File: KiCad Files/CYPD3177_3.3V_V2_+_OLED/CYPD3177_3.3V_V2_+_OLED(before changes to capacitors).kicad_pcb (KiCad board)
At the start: 4 copper layers, 64 x 17 mm, 93 parts, among them IC1 TPS16630RGER, IC2 TPS22992SRXNR, J1 USB_C_USB2.0_16P, J2 Conn_01x02_Pin, J3 Conn_02x05_Odd_Even, J4 Conn_02x05_Odd_Even, J5 0.91 OLED, J6 QWIIC, J7 Conn_01x05, J8 I2C_Header, Q1 DMC2990UDJ-7, SW1 GT-TC0060-H050-L1, SW2 B3U-1000P, U1 TCA9406DC, U2 INA238, U3 XC6220B331PR-G, U4 TPS62933DRLR, U5 AON7534, U6 AP33772S, U7 AON7534, U8 TPS2117DRL, U9 ATtiny3217-M

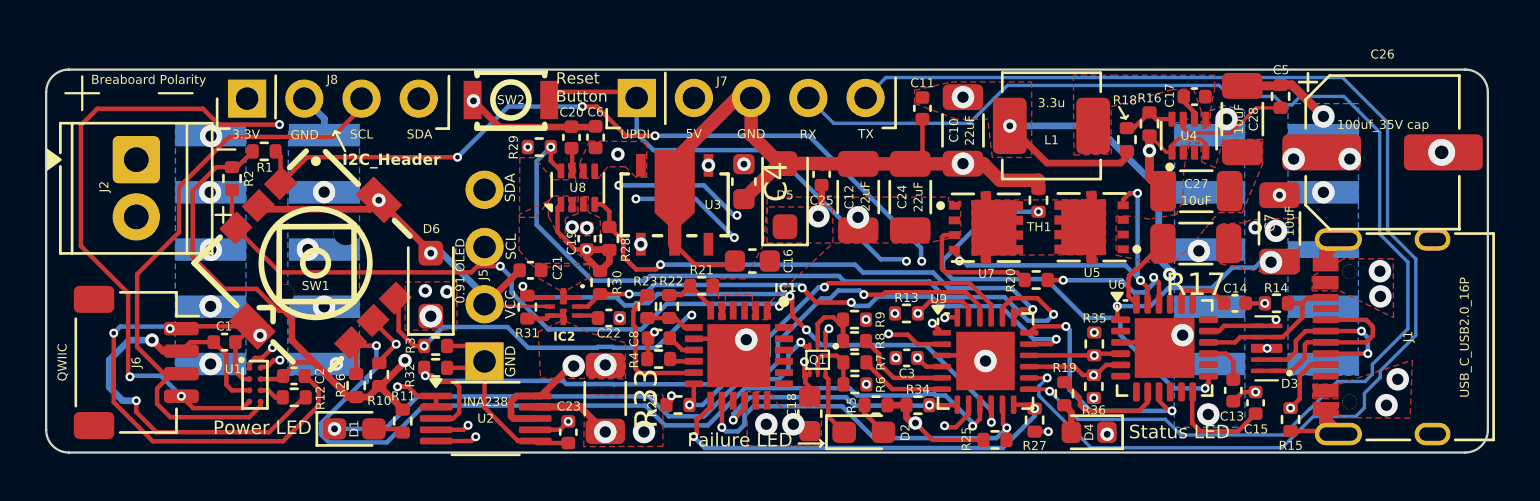
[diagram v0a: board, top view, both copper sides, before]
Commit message: finshed pcb, assigning part numbers
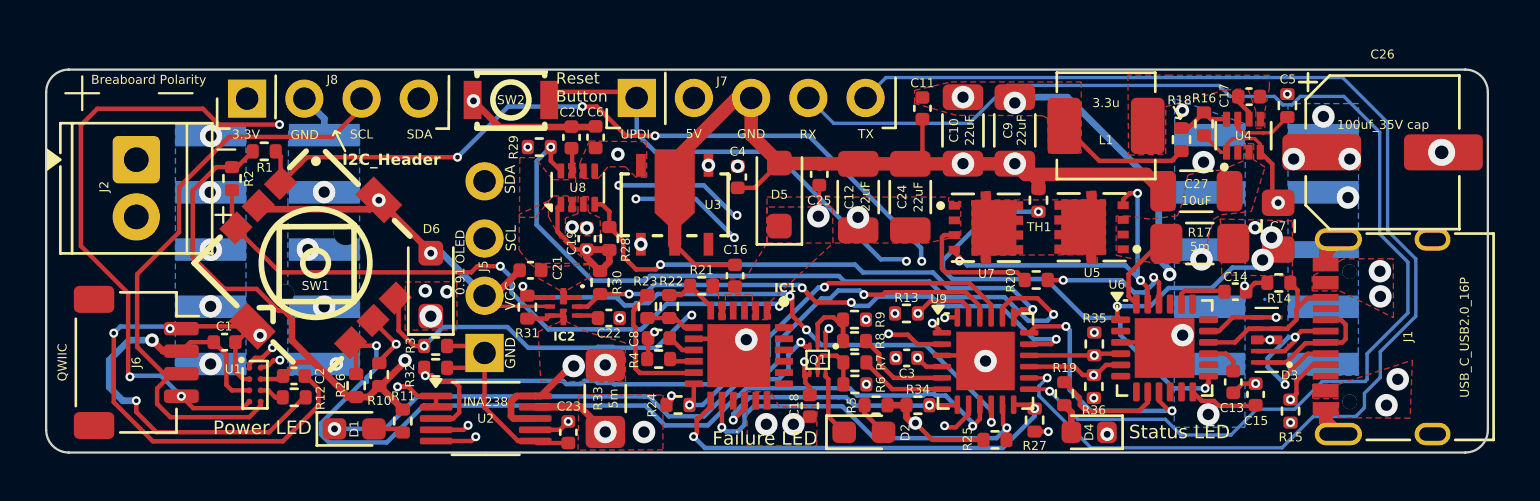
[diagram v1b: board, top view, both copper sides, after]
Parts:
- removed C28: 10uF, Capacitor_SMD:C_1206_3216Metric
- added C9: 22uF, Capacitor_SMD:C_1206_3216Metric, F.Cu at (142.0, 82.7)
- C16, C4: footprint Capacitor_SMD:C_0603_1608Metric -> Capacitor_SMD:C_0402_1005Metric
- C18: value 1uF -> 100uF; footprint Capacitor_SMD:C_0603_1608Metric -> Capacitor_SMD:C_0402_1005Metric
- C20: value 100nF -> 100uF
- C6: value 4.7uF -> 10uF
- C7: footprint Capacitor_SMD:C_1206_3216Metric -> Capacitor_SMD:C_0805_2012Metric_Pad1.18x1.45mm_HandSolder
- C8: value 22nF -> 10uF
- R17, R33: footprint Resistor_SMD:R_1206_3216Metric -> Inductor_SMD:L_1206_3216Metric_Pad1.42x1.75mm_HandSolder
- moved L1 2.42 mm to (146.1, 82.5)
- moved C17 2.42 mm to (152.4, 81.2)
- moved R16 2.42 mm to (150.4, 82.4)
- moved R18 2.42 mm to (149.4, 83.1)
- moved U4 2.42 mm to (152.2, 82.9)
- moved C16 1.01 mm to (129.6, 89.2), turned to 90 degrees
- moved R14 0.91 mm to (153.7, 89.5)
- moved C14 0.52 mm to (151.8, 89.9)
- moved C5 0.51 mm to (154.1, 81.6)
- moved C13 0.38 mm to (151.7, 93.9)
- moved C15 0.38 mm to (152.7, 94.4)
- moved D3 0.38 mm to (153.2, 92.0)
- moved J5 0.38 mm to (155.0, 94.8)
- moved R15 0.38 mm to (154.2, 95.2)
- moved C18 0.35 mm to (132.9, 94.9)
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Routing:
- net /Power/VBUS_Finale: track 15.7 -> 19.5 mm, vias 7 -> 8
- net /Power/USB_P: track 8.75 -> 5.95 mm
- net Net-(U4-SS): track 5.26 -> 2.97 mm
- net /Power/V18: track 4.68 -> 3.06 mm
- net /Power/USB_N: track 8.43 -> 9.18 mm
- net GND: track 122.3 -> 121.5 mm, vias 35 -> 37
- net /Power/CC1: track 11.7 -> 11.0 mm
- net /Power/CC2: track 7.03 -> 7.62 mm
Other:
- board text removed: "10uF"
